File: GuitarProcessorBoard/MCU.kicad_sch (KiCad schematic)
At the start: 101 parts, among them J301 SWD Header, J302 PWR, J303 TAP, J304 MODE, J305 BYP, J306 EXP, J307 ScopeGroundLoop, SW301 RST, SW302 BOOT, SW303 ENC, SW304 BACK, U301 STM32H7B0VBT6, U302 TPS63070, U303 SSD1306_OLED_128x64, U304 74HC595, Y301 32MHz, Y302 32.768kHZ

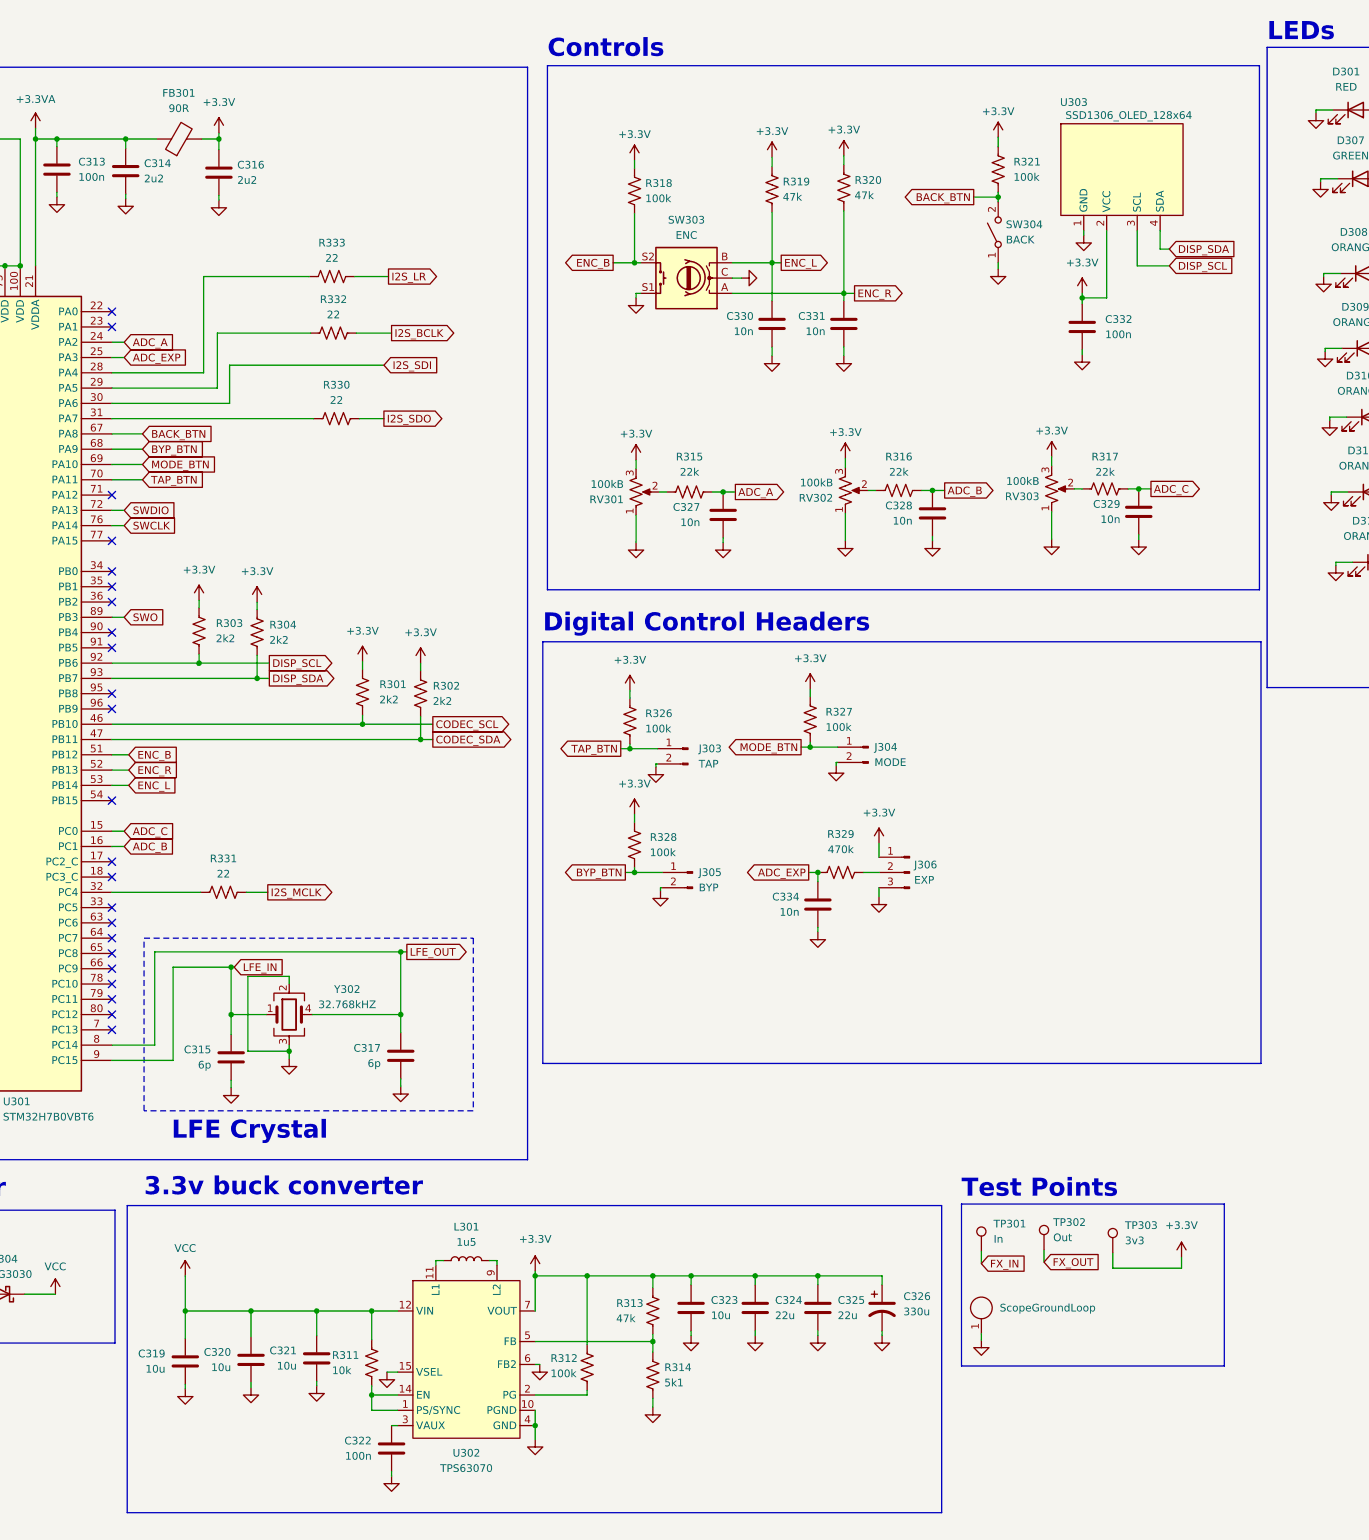
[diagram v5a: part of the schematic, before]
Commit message: removed encoder and back btn
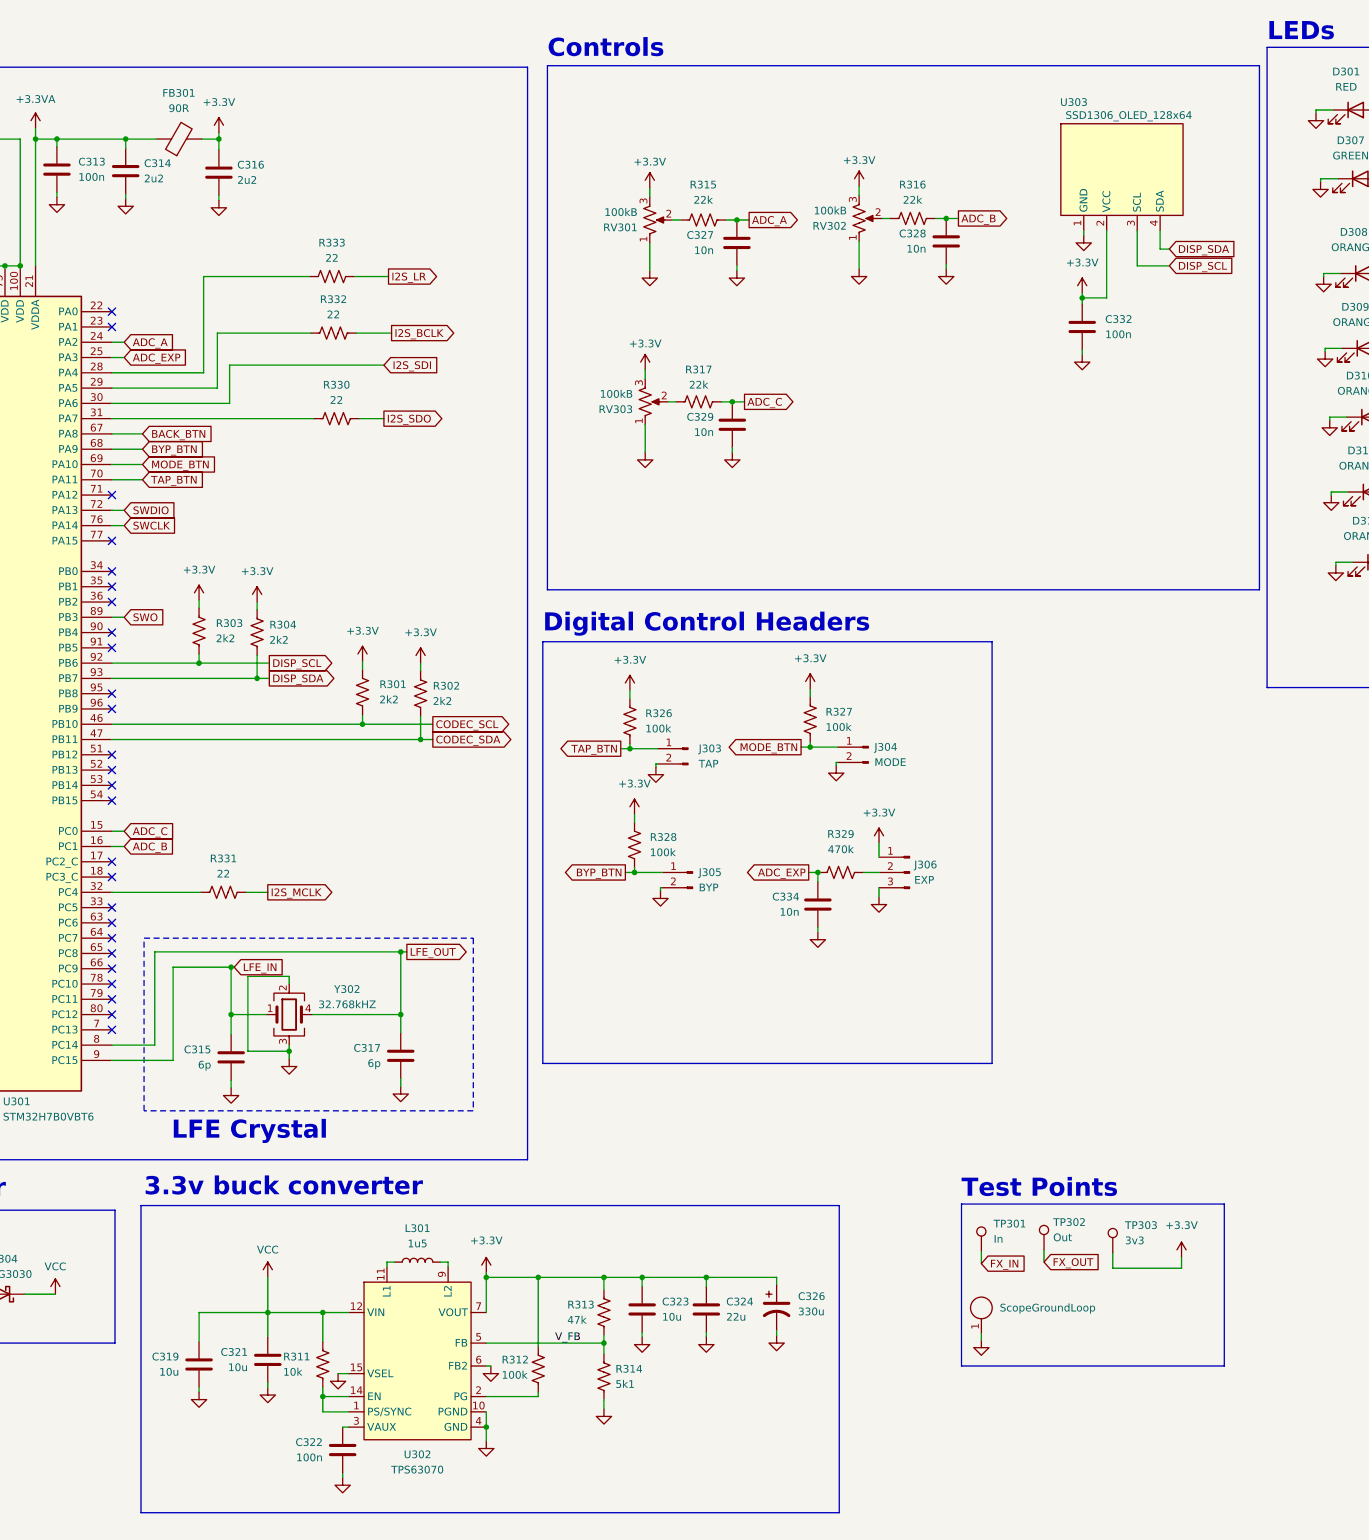
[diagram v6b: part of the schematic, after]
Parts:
- removed C320: 10u, Capacitor_SMD:C_0805_2012Metric, symbol Device:C
- removed C325: 22u, Capacitor_SMD:C_0805_2012Metric, symbol Device:C
- removed C330, C331: 10n, Capacitor_SMD:C_0805_2012Metric, symbol Device:C
- removed R318, R321: 100k, Resistor_SMD:R_0805_2012Metric, symbol Device:R_US
- removed R319, R320: 47k, Resistor_SMD:R_0805_2012Metric, symbol Device:R_US
- removed SW303: ENC, Rotary_Encoder:RotaryEncoder_Alps_EC11E-Switch_Vertical_H20mm_5Pin, symbol Device:RotaryEncoder_Switch
- removed SW304: BACK, Button_Switch_THT:SW_PUSH_6mm, symbol Switch:SW_SPST
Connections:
- net V_FB: now reaches R313.2, R314.1, U302.5 (FB)
- net ENC_B: no longer names the net of U301.51 (PB12)
- net ENC_L: no longer names the net of U301.53 (PB14)
- net ENC_R: no longer names the net of U301.52 (PB13)
- no-connect marks 52 -> 55
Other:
- moved on the sheet: C321, C322, C323, C324, C326, C327, C328, C329, L301, R311, R312, R313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

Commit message: first layout
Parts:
- removed C305: 100n, Capacitor_SMD:C_0805_2012Metric, symbol Device:C
- added D302: ORANGE, LED_THT:LED_D3.0mm, symbol Device:LED
- added R318: 470, Resistor_SMD:R_0805_2012Metric, symbol Device:R_US
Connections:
- net GND: now also D302.1 (K)
- net LED_A1: now also U304.5 (QF); no longer U304.2 (QC)
- net LED_A2: now also U304.4 (QE); no longer U304.3 (QD)
- net LED_A3: now also U304.3 (QD); no longer U304.4 (QE)
- net LED_A4: now also U304.2 (QC); no longer U304.5 (QF)
- net LED_A5: now also U304.1 (QB); no longer U304.6 (QG)
- net LED_BYPASS: now also U304.7 (QH); no longer U304.1 (QB)
- net LED_TEMPO: now also U304.6 (QG); no longer U304.15 (QA)
- net BACK_BTN: no longer names the net of U301.67 (PA8)
- new net: D302.2 (A), R318.1
- new net LED_A6: R318.2, U304.15 (QA)
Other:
- moved on the sheet: C303, C304, C333, R305, U304

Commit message: routing rd one
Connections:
- net LFE_IN: now also Y302.4; no longer Y302.1
- net LFE_OUT: now also Y302.1; no longer Y302.4
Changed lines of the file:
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@@
 		(lib_id "Device:Crystal_GND23")
 		(at 189.738 179.324 0)
+		(mirror y)
 		(unit 1)
 		(exclude_from_sim no)
@@
 		(on_board yes)
 		(dnp no)
-		(fields_autoplaced yes)
 		(property "Reference" "Y302"
-			(at 199.39 175.1331 0)
+			(at 199.644 173.228 0)
 			(effects
 				(font
@@
 		)
 		(property "Value" "32.768kHZ"
-			(at 199.39 177.6731 0)
+			(at 199.644 175.768 0)
 			(effects
 				(font
